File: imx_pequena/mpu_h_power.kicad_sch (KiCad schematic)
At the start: 1 part, among them U1 MCIMX6Z0DVM09AB

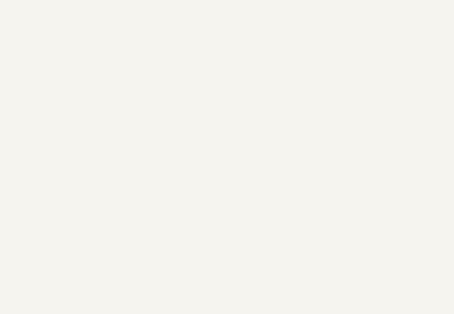
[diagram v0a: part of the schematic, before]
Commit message: Power Update
Added 3v3 and 1.35V switchers
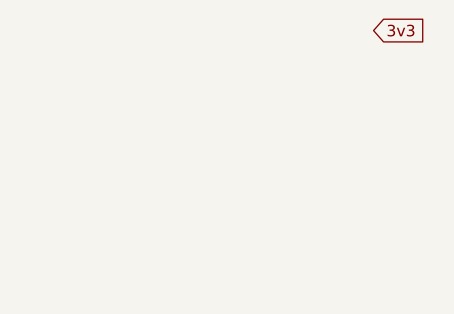
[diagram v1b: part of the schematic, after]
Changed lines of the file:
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@@
 (kicad_sch (version 20211123) (generator eeschema)
   (paper "A4")
+  (global_label "3v3" (shape input) (at 201.93 44.45 0) (fields_autoplaced)
+    (effects (font (size 1.27 1.27)) (justify left))
+    (property "Intersheet References" "${INTERSHEET_REFS}" (id 0) (at 207.7298 44.3706 0)
+      (effects (font (size 1.27 1.27)) (justify left) hide)
+    )
+  )
   (symbol (lib_id "MCIMX6Z0DVM09AB:MCIMX6Z0DVM09AB") (at 135.89 86.36 0) (unit 8)
     (in_bom yes) (on_board yes) (fields_autoplaced)

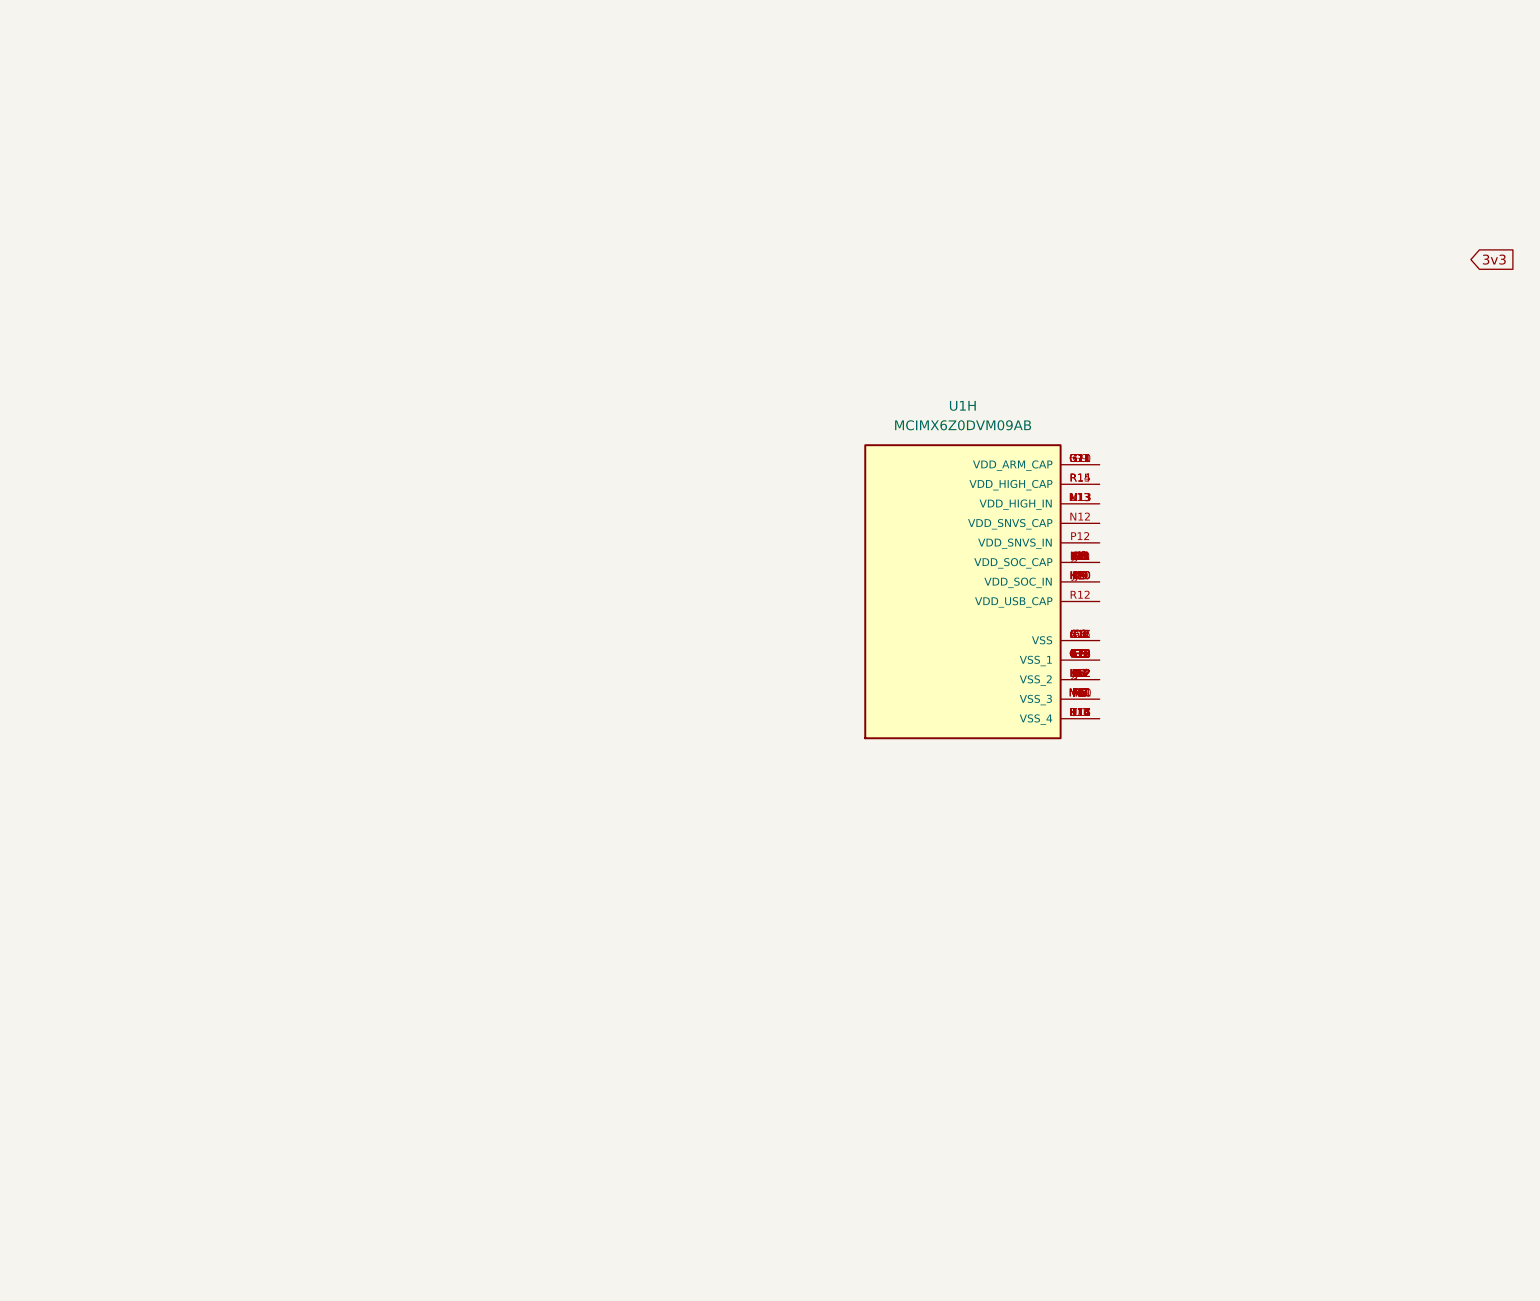
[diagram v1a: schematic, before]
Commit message: Power upates
Added connections to power pins and decoupling caps
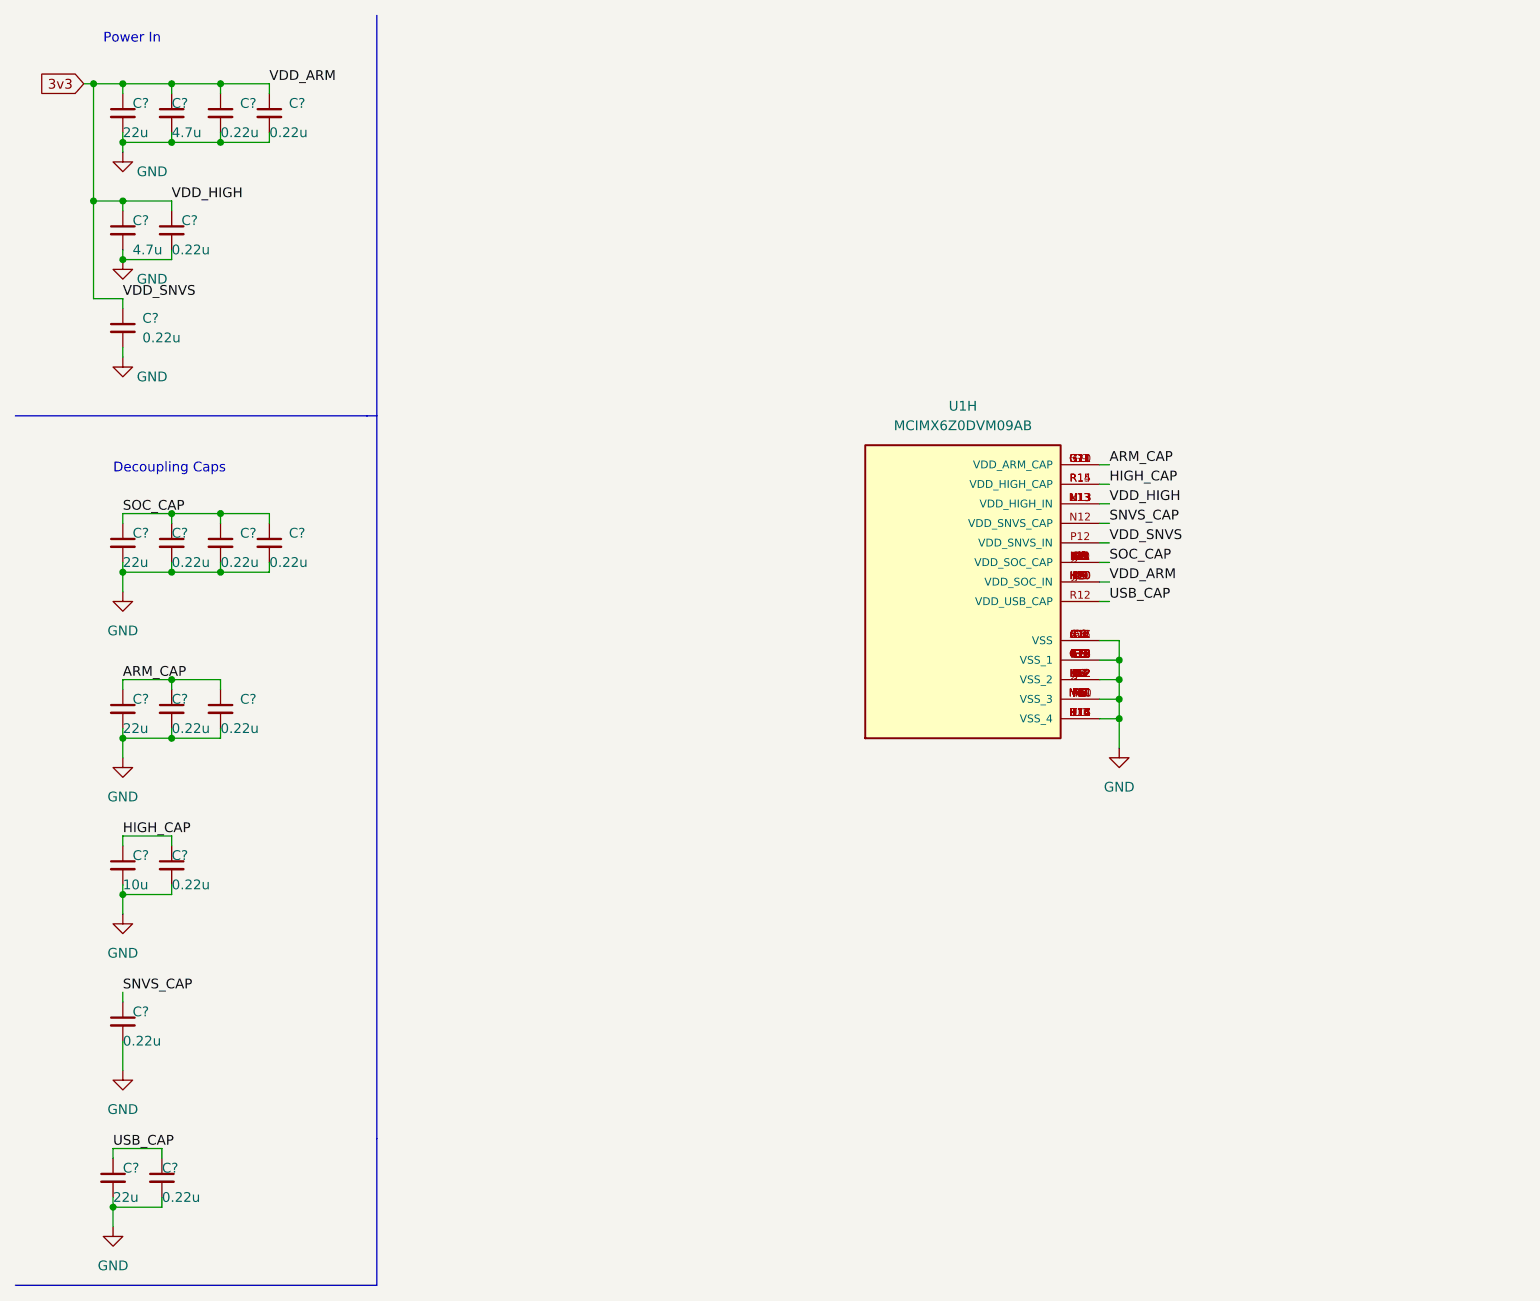
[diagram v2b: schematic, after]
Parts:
- added C? (x12): 0.22u, symbol Device:C_Small
- added C? (x2): 4.7u, symbol Device:C_Small
- added C? (x4): 22u, symbol Device:C_Small
- added C?: 10u, symbol Device:C_Small
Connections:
- net 3v3: now also U1.H10 (VDD_SOC_IN), U1.H9 (VDD_SOC_IN), U1.J10 (VDD_SOC_IN), U1.J9 (VDD_SOC_IN), U1.K10 (VDD_SOC_IN), U1.K9 (VDD_SOC_IN), U1.L13 (VDD_HIGH_IN), U1.M13 (VDD_HIGH_IN), U1.N13 (VDD_HIGH_IN), U1.P12 (VDD_SNVS_IN), C?.1, C?.1, C?.1, C?.1, C?.1, C?.1, C?.1
- net GND: now reaches U1.A1 (VSS), U1.A17 (VSS), U1.C11 (VSS), U1.C15 (VSS), U1.C3 (VSS), U1.C7 (VSS), U1.E11 (VSS), U1.E8 (VSS), U1.F6 (VSS), U1.F7 (VSS)
- net GND: now also U1.F10 (VSS_1), U1.F11 (VSS_1), U1.F12 (VSS_1), U1.F8 (VSS_1), U1.F9 (VSS_1), U1.G12 (VSS_1), U1.G15 (VSS_1), U1.G3 (VSS_1), U1.G5 (VSS_1), U1.G7 (VSS_1), U1.H12 (VSS_2), U1.H7 (VSS_2), U1.J12 (VSS_2), U1.J5 (VSS_2), U1.J7 (VSS_2), U1.K12 (VSS_2), U1.K7 (VSS_2), U1.L12 (VSS_2), U1.L3 (VSS_2), U1.L7 (VSS_2), U1.M10 (VSS_3), U1.M11 (VSS_3), U1.M7 (VSS_3), U1.M8 (VSS_3), U1.M9 (VSS_3), U1.N3 (VSS_3), U1.N5 (VSS_3), U1.R11 (VSS_4), U1.R16 (VSS_4), U1.R17 (VSS_4), U1.R3 (VSS_3), U1.R5 (VSS_3), U1.R7 (VSS_3), U1.T14 (VSS_4), U1.U1 (VSS_4), U1.U14 (VSS_4), U1.U17 (VSS_4), C?.2, C?.2, C?.2, C?.2, C?.2, C?.2, C?.2, C?.2, C?.2, C?.2, C?.2, C?.2, C?.2, C?.2, C?.2, C?.2, C?.2, C?.2, C?.2
- net ARM_CAP: now reaches U1.G10 (VDD_ARM_CAP), U1.G11 (VDD_ARM_CAP), U1.G9 (VDD_ARM_CAP), U1.H11 (VDD_ARM_CAP)
- net ARM_CAP: now also C?.1, C?.1, C?.1
- net SOC_CAP: now reaches U1.G8 (VDD_SOC_CAP), U1.H8 (VDD_SOC_CAP), U1.J11 (VDD_SOC_CAP), U1.J8 (VDD_SOC_CAP), U1.K11 (VDD_SOC_CAP), U1.K8 (VDD_SOC_CAP), U1.L10 (VDD_SOC_CAP), U1.L11 (VDD_SOC_CAP), U1.L8 (VDD_SOC_CAP), U1.L9 (VDD_SOC_CAP)
- net SOC_CAP: now also C?.1, C?.1, C?.1, C?.1
- net SNVS_CAP: now reaches U1.N12 (VDD_SNVS_CAP)
- net SNVS_CAP: now also C?.1
- net USB_CAP: now reaches U1.R12 (VDD_USB_CAP)
- net USB_CAP: now also C?.1, C?.1
- net HIGH_CAP: now reaches U1.R14 (VDD_HIGH_CAP), U1.R15 (VDD_HIGH_CAP)
- net HIGH_CAP: now also C?.1, C?.1
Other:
- note added: "Decoupling Caps"
- note added: "Power In"

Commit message: Part Assignment
Assigned GPIOs and assigned footprints to most parts
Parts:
- C66, C67, C68, C70, C71, C72, C75: renamed from C?; footprint (none) -> Capacitor_SMD:C_0805_2012Metric
- C69, C73, C74, C76, C77, C78, C79, C80, C81, C82, C83, C84: renamed from C?; footprint (none) -> Capacitor_SMD:C_0402_1005Metric
